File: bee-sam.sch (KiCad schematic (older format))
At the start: 30 parts, among them J1 Conn_01x02_Male, J2 Conn_01x02_Male, J3 Conn_01x02_Male, J4 Conn_01x02_Male, J6 Screw_Terminal_01x02, J7 Conn_01x02, J8 Conn_01x02, U2 LM380N

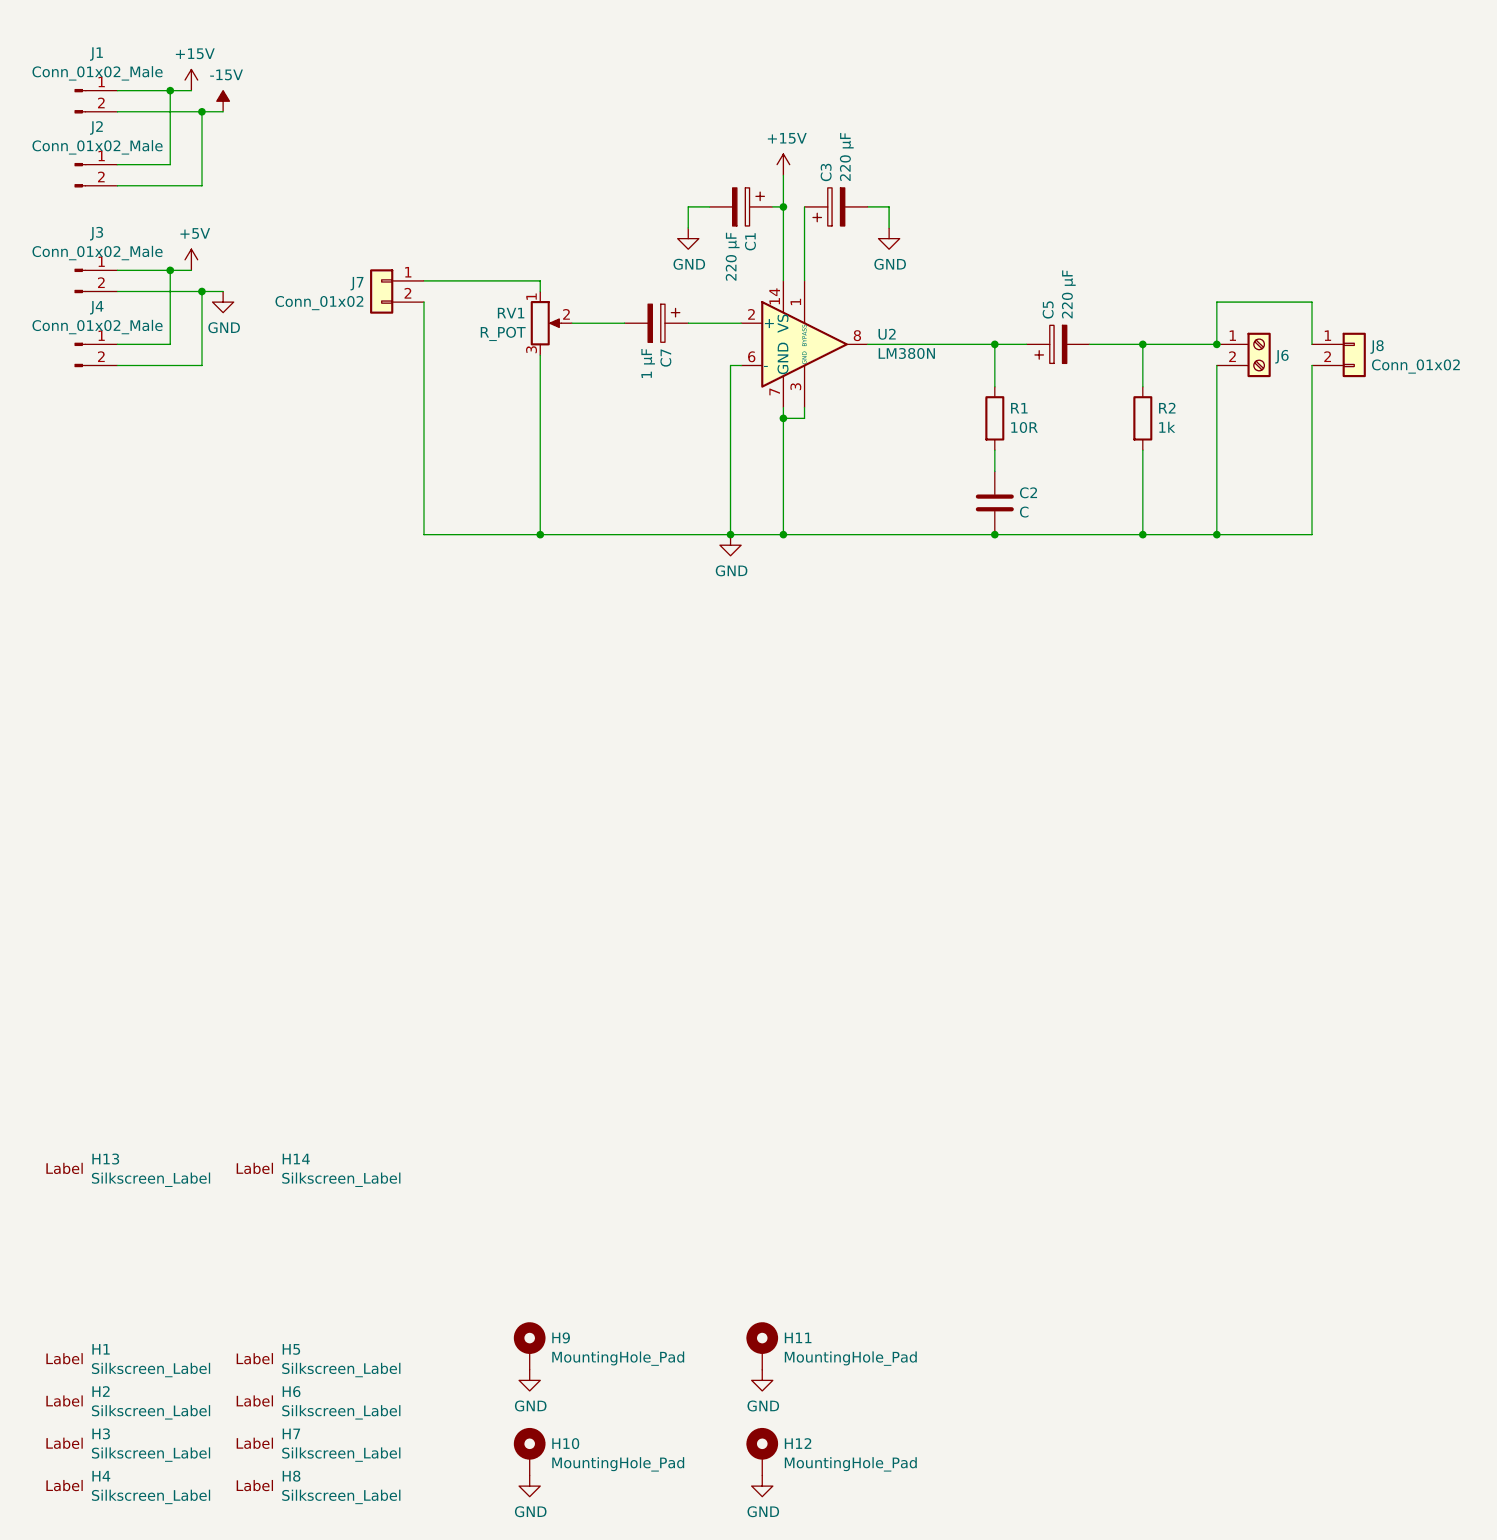
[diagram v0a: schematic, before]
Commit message: Refactoring
* Replace capacitor footprints with more versatile footprints
* Print device values on pcb
* Adapt spacings between components and heatsink
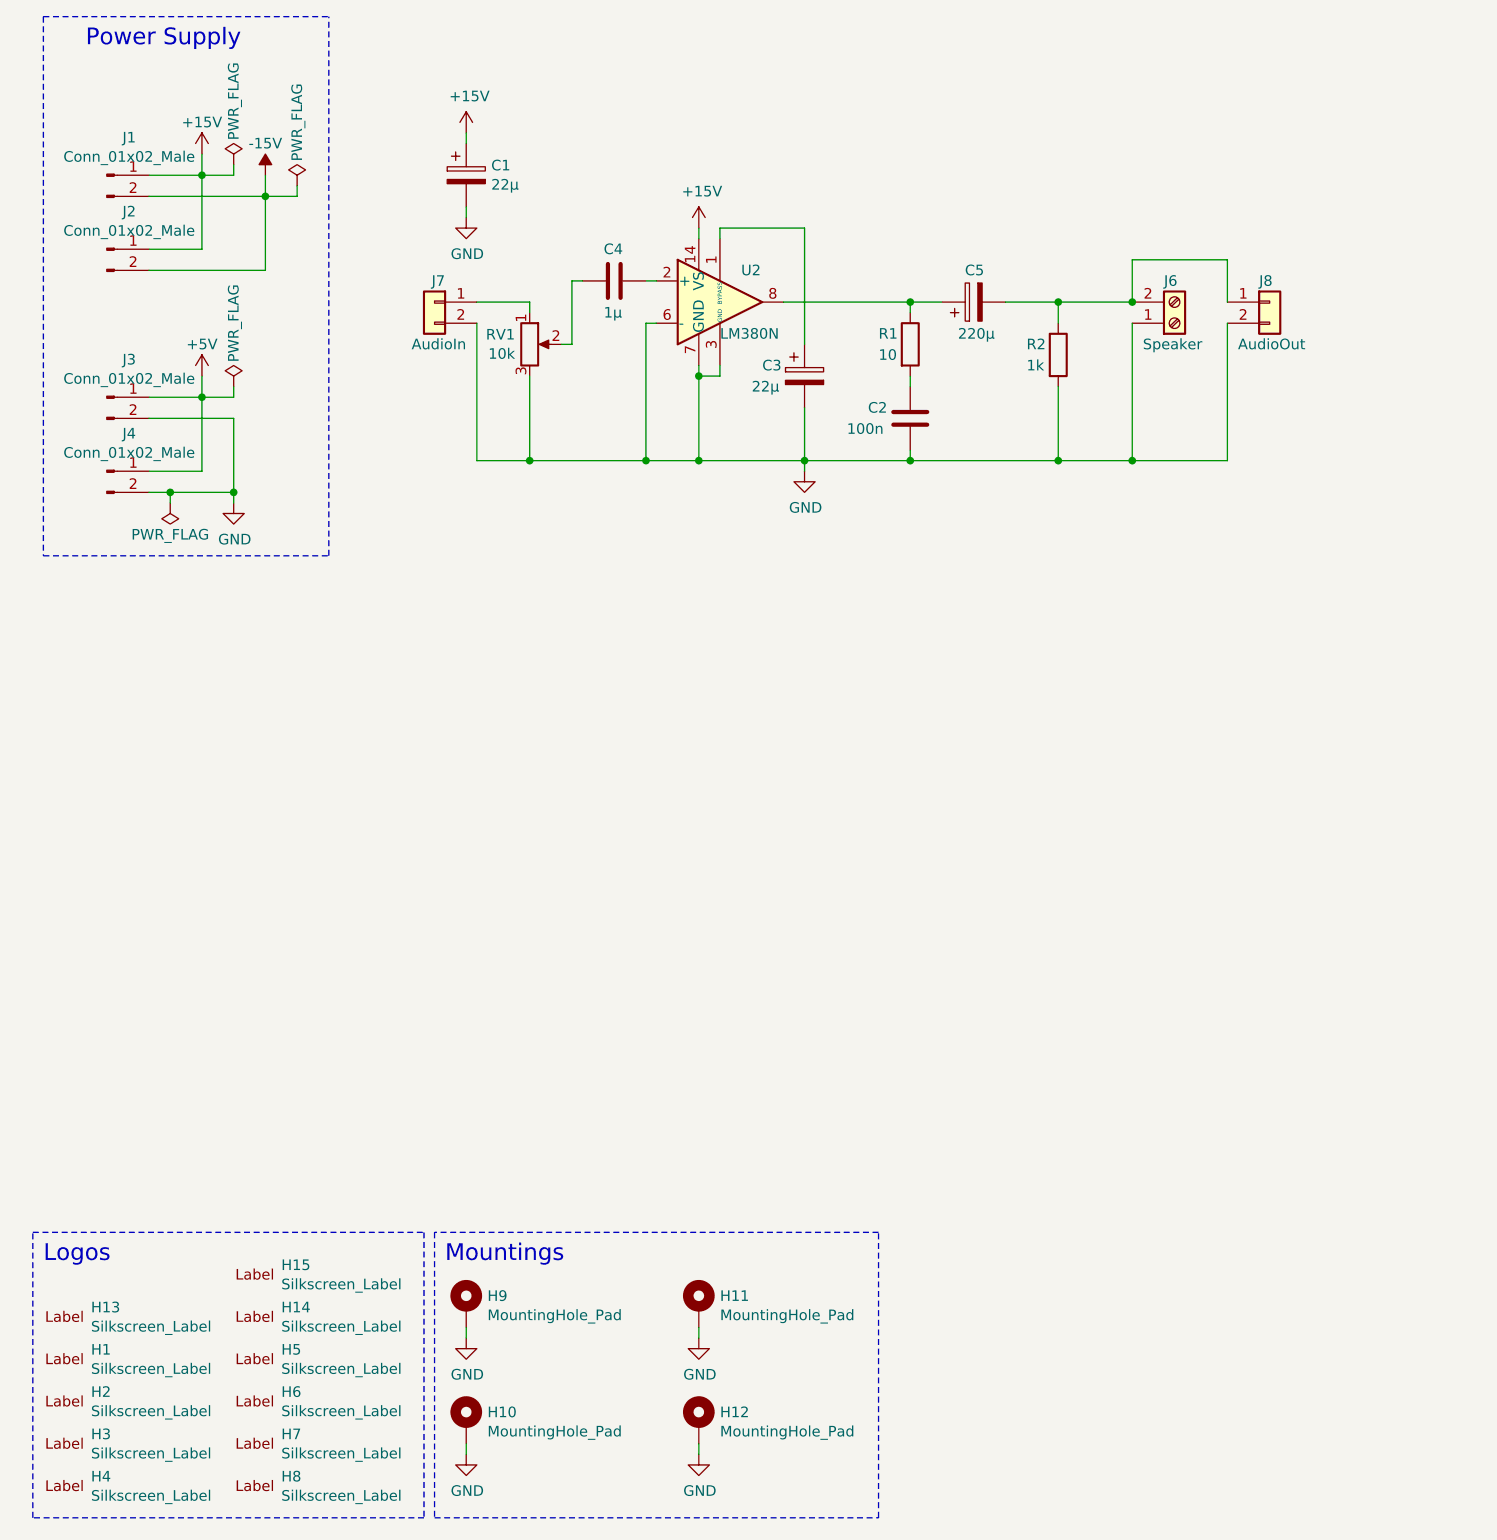
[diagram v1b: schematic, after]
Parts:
- removed C7: 1 µF, Capacitor_THT:CP_Radial_D8.0mm_P5.00mm, symbol Device:CP
- added C4: 1µ, Capacitor_THT:C_Rect_L7.2mm_W3.0mm_P5.00mm_FKS2_FKP2_MKS2_MKP2, symbol Device:C
- added H15: Silkscreen_Label, Symbol-emt:EMT-Logo_8.2x4.1mm_Silkscreen, symbol Mechanical-bee:Silkscreen_Label
- C1, C3: value 220 µF -> 22µ; footprint Capacitor_THT:CP_Radial_D8.0mm_P5.00mm -> kicad-footprints-bee:CP_Radial_D8.0mm_P2.50mm_P3.80mm_P5.00mm
- C2: value C -> 100n
- C5: value 220 µF -> 220µ; footprint Capacitor_THT:CP_Radial_D8.0mm_P5.00mm -> kicad-footprints-bee:CP_Radial_D8.0mm_P2.50mm_P3.80mm_P5.00mm
- J6: value Screw_Terminal_01x02 -> Speaker
- J7: value Conn_01x02 -> AudioIn
- J8: value Conn_01x02 -> AudioOut
- R1: value 10R -> 10
- RV1: value R_POT -> 10k
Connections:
- net GND: now also J6.1 (Pin_1); no longer J6.2 (Pin_2)
- net at U2.2 (+): now also C4.1
- net at C5.2, J8.1 (Pin_1), R2.1: now also J6.2 (Pin_2); no longer J6.1 (Pin_1)
- net at RV1.2: now also C4.2
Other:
- note added: "Logos"
- note added: "Mountings"
- note added: "Power Supply"
- moved on the sheet: C2, C3, C5, H10, H11, H12, H13, H14, H9, J1, J2, J3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
